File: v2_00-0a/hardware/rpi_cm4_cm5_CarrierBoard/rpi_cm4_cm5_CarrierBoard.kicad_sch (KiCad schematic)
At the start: 0 parts

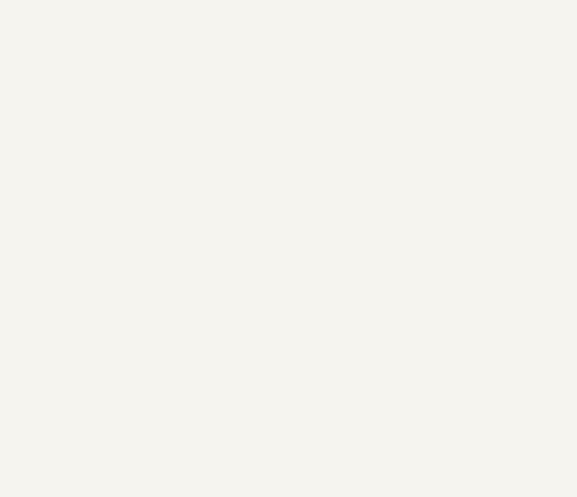
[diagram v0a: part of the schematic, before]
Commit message: Add power supply schematic sheet
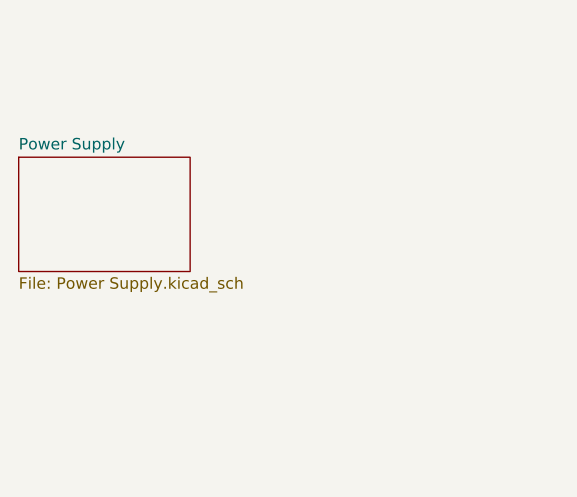
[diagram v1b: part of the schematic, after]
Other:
- added sheet Power Supply (Power Supply.kicad_sch)
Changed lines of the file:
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@@
+		)
+	)
+	(sheet
+		(at 101.6 177.8)
+		(size 19.05 12.7)
+		(exclude_from_sim no)
+		(in_bom yes)
+		(on_board yes)
+		(dnp no)
+		(fields_autoplaced yes)
+		(stroke
+			(width 0.1524)
+			(type solid)
+		)
+		(fill
+			(color 0 0 0 0.0000)
+		)
+		(property "Sheetname" "Power Supply"
+			(at 101.6 177.0884 0)
+			(effects
+				(font
+					(size 1.27 1.27)
+				)
+				(justify left bottom)
+			)
+		)
+		(property "Sheetfile" "Power Supply.kicad_sch"
+			(at 101.6 191.0846 0)
+			(effects
+				(font
+					(size 1.27 1.27)
+				)
+				(justify left top)
+			)
+		)
+		(instances
+			(project "rpi_cm4_cm5_CarrierBoard"
+				(path "/7dcdf741-90ca-4333-848c-806f4d64158e"
+					(page "5")
+				)
+			)
 		)
 	)

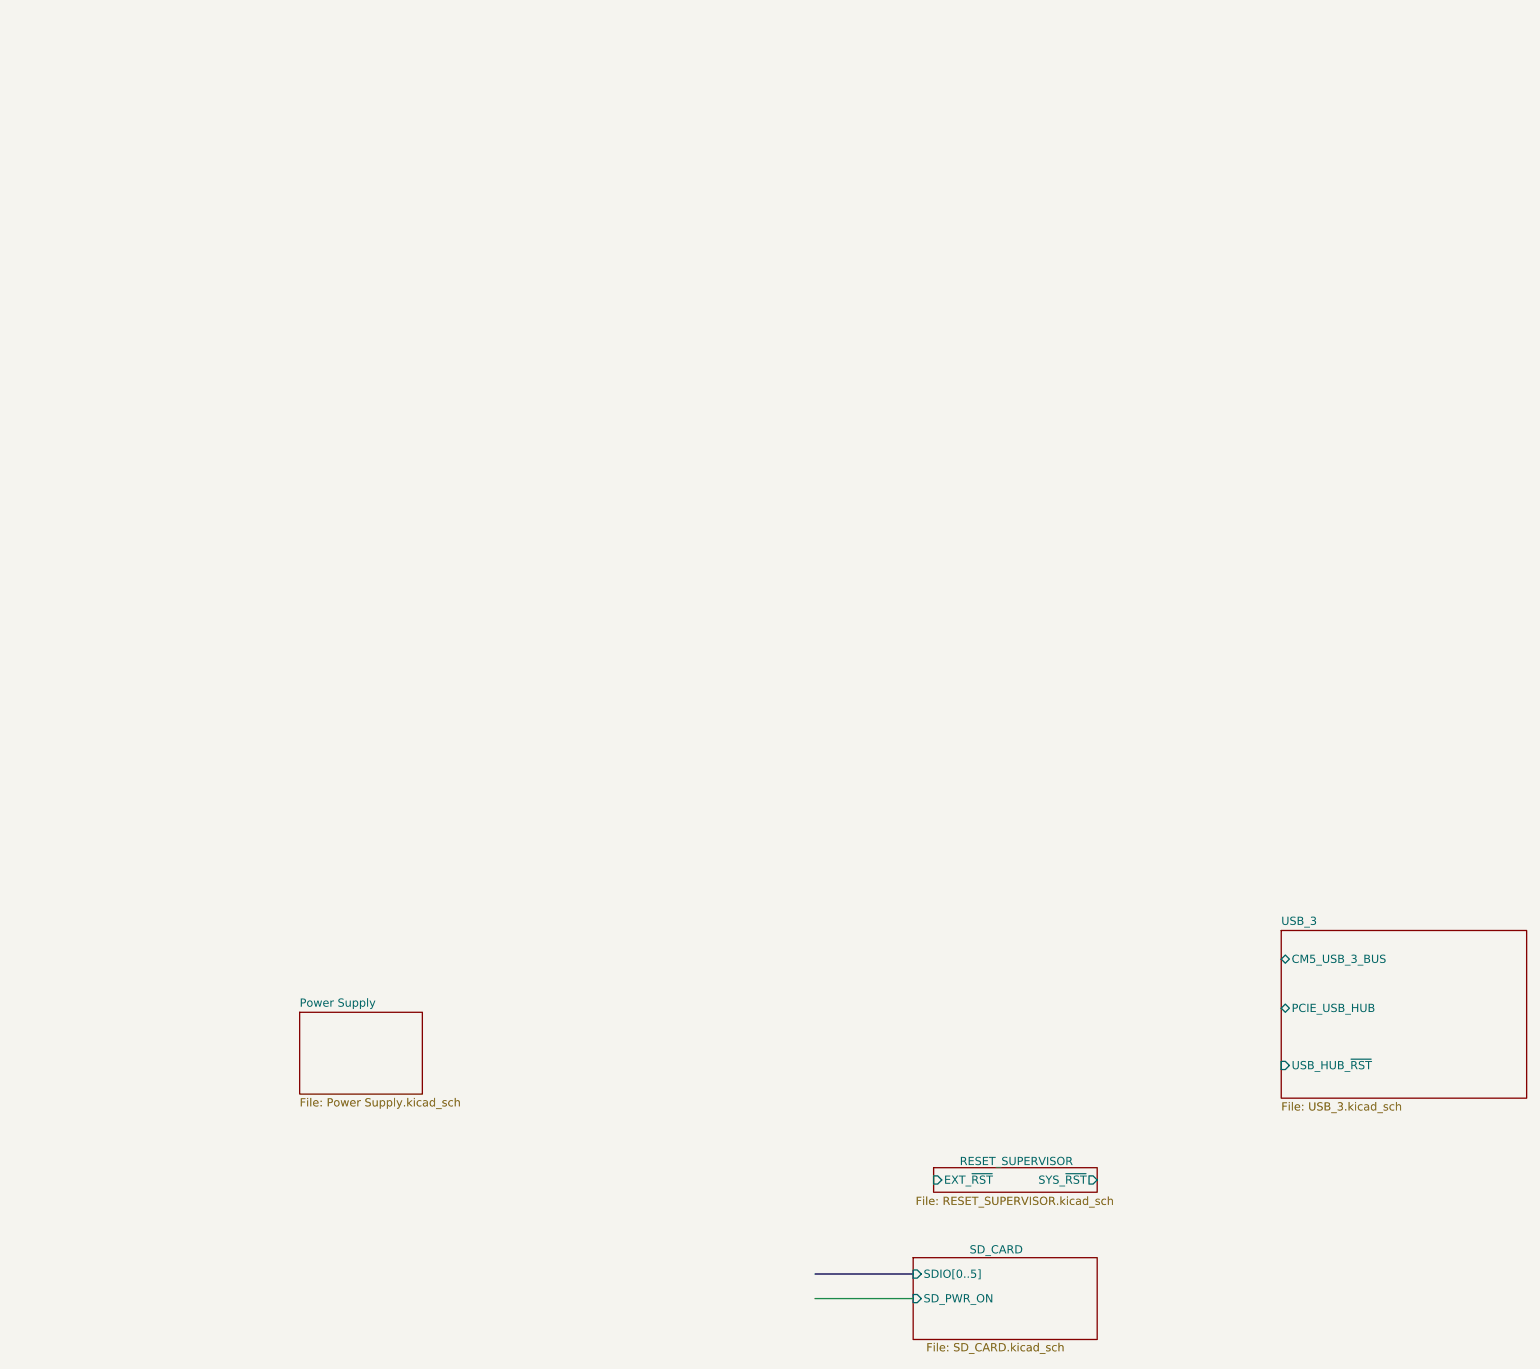
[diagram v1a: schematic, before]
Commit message: Add schematic pages for SOM_CONN_A/B, DSI to LVDS bridge, Ethernet and HDMI
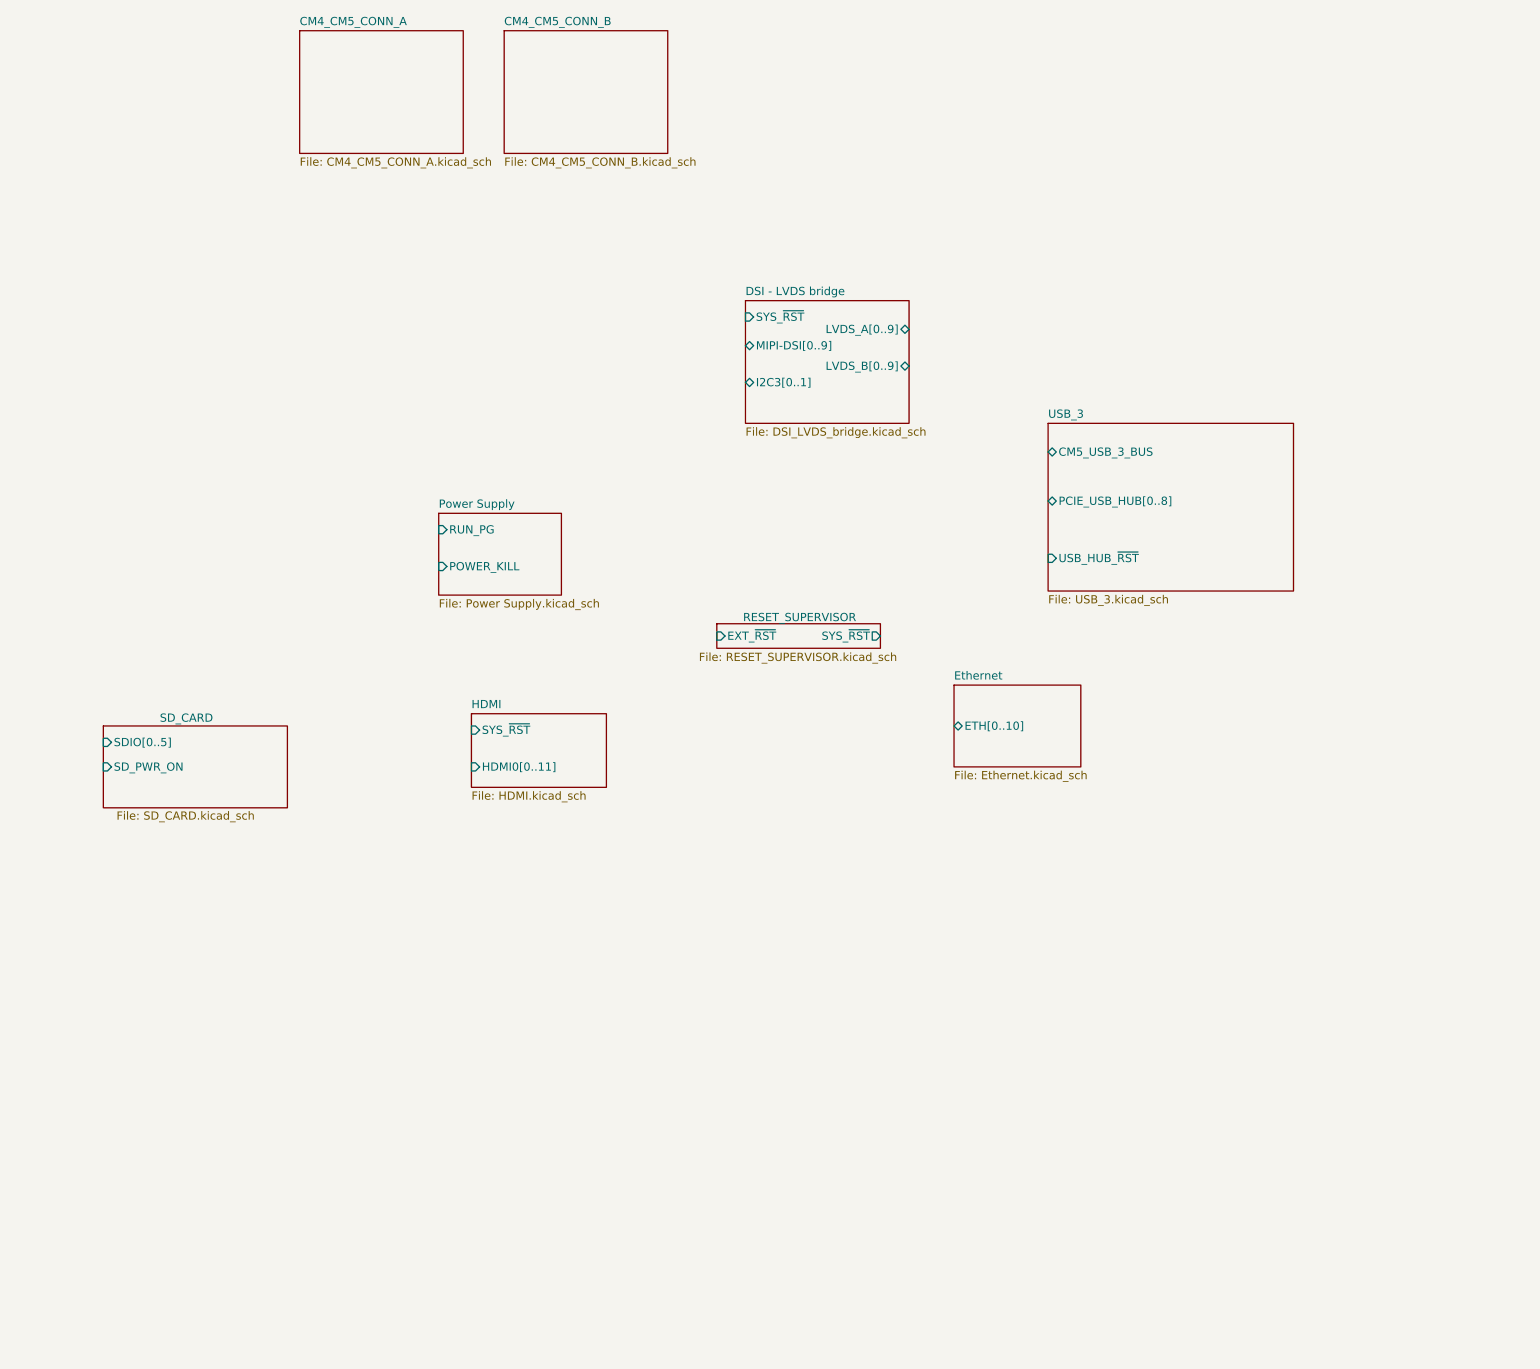
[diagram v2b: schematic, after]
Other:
- added sheet CM4_CM5_CONN_A (CM4_CM5_CONN_A.kicad_sch)
- added sheet CM4_CM5_CONN_B (CM4_CM5_CONN_B.kicad_sch)
- added sheet DSI - LVDS bridge (DSI_LVDS_bridge.kicad_sch)
- added sheet Ethernet (Ethernet.kicad_sch)
- added sheet HDMI (HDMI.kicad_sch)
- sheet Power Supply ports: added POWER_KILL, RUN_PG; removed none
- sheet USB_3 ports: added PCIE_USB_HUB[0..8]; removed PCIE_USB_HUB

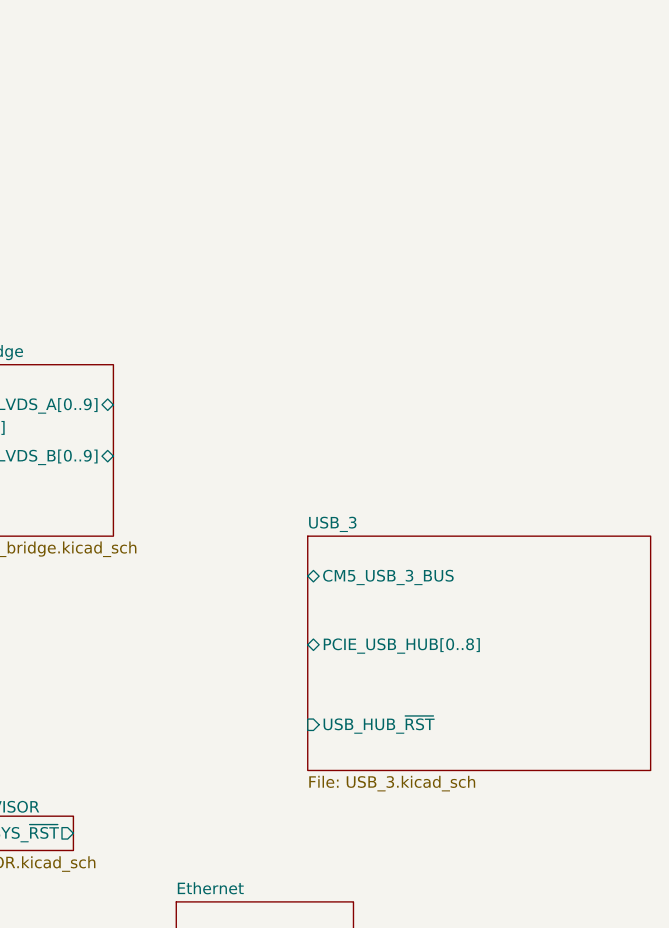
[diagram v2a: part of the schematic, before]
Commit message: Update schematics (several new hierarchical pages, updates bus labels)
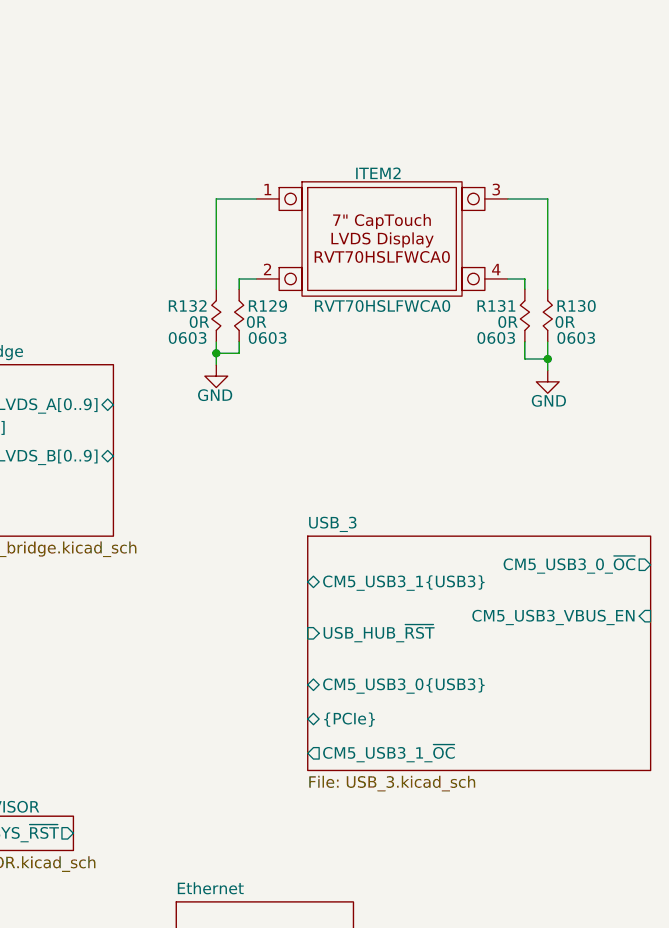
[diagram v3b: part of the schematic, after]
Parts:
- added ITEM2: RVT70HSLFWCA0, footprint:RVT70HSLFWCA0, symbol KicadCompDb:Miscellaneous/MISC_00003
- added R129, R130, R131, R132: 0R, footprint:RES_0603, symbol KicadCompDb:Resistors/RES_SMT_00021
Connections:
- new net: ITEM2.3, R130.1
- new net: ITEM2.1, R132.1
- new net: ITEM2.2, R129.1
- new net: ITEM2.4, R131.1
- new net GND: R129.2, R130.2, R131.2, R132.2
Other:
- sheet USB_3 ports: added CM5_USB3_0_~{OC}, CM5_USB3_0{USB3}, CM5_USB3_1_~{OC}, CM5_USB3_1{USB3}, CM5_USB3_VBUS_EN, {PCIe}; removed CM5_USB_3_BUS, PCIE_USB_HUB[0..8]
